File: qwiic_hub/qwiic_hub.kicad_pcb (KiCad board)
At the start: 2 copper layers, 22.8 x 15.6 mm, 10 parts, among them J1 Conn_01x04_Pin, J2 Conn_01x04_Pin, J3 Conn_01x04_Pin, J4 Conn_01x04_Pin, J5 Conn_01x04_Pin, J6 Conn_01x04_Socket, X1 QWIIC Logo

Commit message: Cleaned up the layout.
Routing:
- net /GND: track 51.4 -> 55.5 mm
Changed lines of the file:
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@@
     (fp_line (start 3 -1.675) (end 3 2.575)
       (stroke (width 0.1) (type solid)) (layer "F.Fab"))
-    (pad "1" smd roundrect (at -1.5 -2 90) (size 0.6 1.55) (layers "F.Cu" "F.Paste" "F.Mask") (roundrect_rratio 0.25)
+    (pad "1" thru_hole roundrect (at -1.5 -2 90) (size 0.6 1.55) (drill 0.3) (layers "*.Cu" "F.Paste" "F.Mask") (roundrect_rratio 0.25)
       (net 4 "/GND") (pinfunction "Pin_1") (pintype "passive"))
-    (pad "2" smd roundrect (at -0.5 -2 90) (size 0.6 1.55) (layers "F.Cu" "F.Paste" "F.Mask") (roundrect_rratio 0.25)
+    (pad "2" thru_hole roundrect (at -0.5 -2 90) (size 0.6 1.55) (drill 0.3) (layers "*.Cu" "F.Paste" "F.Mask") (roundrect_rratio 0.25)
       (net 6 "Net-(J1-Pin_2)") (pinfunction "Pin_2") (pintype "passive"))
-    (pad "3" smd roundrect (at 0.5 -2 90) (size 0.6 1.55) (layers "F.Cu" "F.Paste" "F.Mask") (roundrect_rratio 0.25)
+    (pad "3" thru_hole roundrect (at 0.5 -2 90) (size 0.6 1.55) (drill 0.3) (layers "*.Cu" "F.Paste" "F.Mask") (roundrect_rratio 0.25)
       (net 2 "Net-(J1-Pin_3)") (pinfunction "Pin_3") (pintype "passive"))
-    (pad "4" smd roundrect (at 1.5 -2 90) (size 0.6 1.55) (layers "F.Cu" "F.Paste" "F.Mask") (roundrect_rratio 0.25)
+    (pad "4" thru_hole roundrect (at 1.5 -2 90) (size 0.6 1.55) (drill 0.3) (layers "*.Cu" "F.Paste" "F.Mask") (roundrect_rratio 0.25)
       (net 3 "Net-(J1-Pin_4)") (pinfunction "Pin_4") (pintype "passive"))
-    (pad "MP" smd roundrect (at -2.8 1.875 90) (size 1.2 1.8) (layers "F.Cu" "F.Paste" "F.Mask") (roundrect_rratio 0.2083333333))
-    (pad "MP" smd roundrect (at 2.8 1.875 90) (size 1.2 1.8) (layers "F.Cu" "F.Paste" "F.Mask") (roundrect_rratio 0.2083333333))
+    (pad "MP" thru_hole roundrect (at -2.8 1.875 90) (size 1.2 1.8) (drill 0.3) (layers "*.Cu" "F.Paste" "F.Mask") (roundrect_rratio 0.2083333333))
+    (pad "MP" thru_hole roundrect (at 2.8 1.875 90) (size 1.2 1.8) (drill 0.3) (layers "*.Cu" "F.Paste" "F.Mask") (roundrect_rratio 0.2083333333))
     (model "${KICAD6_3DMODEL_DIR}/Connector_JST.3dshapes/JST_SH_SM04B-SRSS-TB_1x04-1MP_P1.00mm_Horizontal.wrl"
       (offset (xyz 0 0 0))
@@
   (segment (start 148.6662 86.3219) (end 148.6662 82.3341) (width 0.3048) (layer "B.Cu") (net 3))
   (segment (start 147.3962 85.3412) (end 147.375 85.32) (width 0.3048) (layer "F.Cu") (net 4))
-  (segment (start 149.287 92.7562) (end 148.0312 92.7562) (width 0.3048) (layer "F.Cu") (net 4))
   (segment (start 139.7254 85.3186) (end 139.7268 85.32) (width 0.3048) (layer "F.Cu") (net 4))
   (segment (start 135.945 85.32) (end 139.724 85.32) (width 0.3048) (layer "F.Cu") (net 4))
   (segment (start 135.945 89.0228) (end 133.985 90.9828) (width 0.3048) (layer "F.Cu") (net 4))
   (segment (start 139.7268 85.32) (end 153.09 85.32) (width 0.3048) (layer "F.Cu") (net 4))
+  (segment (start 151.0492 92.7562) (end 151.0538 92.7608) (width 0.3048) (layer "F.Cu") (net 4))
+  (segment (start 149.287 93.4862) (end 148.971 93.8022) (width 0.3048) (layer "F.Cu") (net 4))
   (segment (start 139.724 85.32) (end 139.7254 85.3186) (width 0.3048) (layer "F.Cu") (net 4))
-  (segment (start 149.287 92.7562) (end 150.7698 92.7562) (width 0.3048) (layer "F.Cu") (net 4))
+  (segment (start 149.287 92.7562) (end 149.287 93.4862) (width 0.3048) (layer "F.Cu") (net 4))
   (segment (start 133.985 90.9828) (end 133.985 93.98) (width 0.3048) (layer "F.Cu") (net 4))
   (segment (start 145.41495 94.6404) (end 144.34825 94.6404) (width 0.3048) (layer "F.Cu") (net 4))
   (segment (start 135.945 85.32) (end 135.945 89.0228) (width 0.3048) (layer "F.Cu") (net 4))
-  (segment (start 150.7698 92.7562) (end 150.7744 92.7608) (width 0.3048) (layer "F.Cu") (net 4))
-  (via (at 150.7744 92.7608) (size 1.016) (drill 0.508) (layers "F.Cu" "B.Cu") (net 4))
-  (via (at 148.082 92.7562) (size 1.016) (drill 0.508) (layers "F.Cu" "B.Cu") (net 4))
+  (segment (start 149.287 92.7562) (end 151.0492 92.7562) (width 0.3048) (layer "F.Cu") (net 4))
+  (segment (start 148.971 93.8022) (end 147.9804 93.8022) (width 0.3048) (layer "F.Cu") (net 4))
+  (via (at 151.0538 92.7608) (size 1.016) (drill 0.508) (layers "F.Cu" "B.Cu") (net 4))
+  (via (at 147.9804 93.8022) (size 1.016) (drill 0.508) (layers "F.Cu" "B.Cu") (net 4))
   (via (at 145.542 94.6404) (size 0.762) (drill 0.381) (layers "F.Cu" "B.Cu") (net 4))
-  (segment (start 147.375 85.32) (end 147.375 90.115) (width 0.3048) (layer "B.Cu") (net 4))
-  (segment (start 153.09 85.32) (end 153.09 90.8262) (width 0.3048) (layer "B.Cu") (net 4))
-  (segment (start 135.9408 85.3242) (end 135.9408 90.2462) (width 0.3048) (layer "B.Cu") (net 4))
+  (segment (start 147.375 85.32) (end 147.375 91.0802) (width 0.3048) (layer "B.Cu") (net 4))
+  (segment (start 153.09 86.3304) (end 151.6634 87.757) (width 0.3048) (layer "B.Cu") (net 4))
+  (segment (start 135.9408 85.3242) (end 135.9408 91.1352) (width 0.3048) (layer "B.Cu") (net 4))
+  (segment (start 153.09 85.32) (end 153.09 86.3304) (width 0.3048) (layer "B.Cu") (net 4))
   (segment (start 141.66 90.9786) (end 141.6558 90.9828) (width 0.3048) (layer "B.Cu") (net 4))
+  (segment (start 151.6634 87.757) (end 151.6634 91.3384) (width 0.3048) (layer "B.Cu") (net 4))
   (segment (start 141.66 85.32) (end 141.66 90.9786) (width 0.3048) (layer "B.Cu") (net 4))
-  (segment (start 147.375 90.115) (end 147.3708 90.1192) (width 0.3048) (layer "B.Cu") (net 4))
   (segment (start 135.945 85.32) (end 135.9408 85.3242) (width 0.3048) (layer "B.Cu") (net 4))
-  (segment (start 153.09 90.8262) (end 153.0858 90.8304) (width 0.3048) (layer "B.Cu") (net 4))
+  (segment (start 147.375 91.0802) (end 147.3454 91.1098) (width 0.3048) (layer "B.Cu") (net 4))
   (segment (start 136.525 90.3732) (end 136.525 93.98) (width 0.3048) (layer "F.Cu") (net 5))
   (segment (start 144.907 90.4494) (end 144.907 88.138) (width 0.3048) (layer "F.Cu") (net 5))
@@
   (via (at 137.3886 86.4362) (size 1.016) (drill 0.508) (layers "F.Cu" "B.Cu") (net 5))
   (via (at 137.3632 84.328) (size 1.016) (drill 0.508) (layers "F.Cu" "B.Cu") (net 5))
-  (via (at 144.8054 88.0364) (size 1.016) (drill 0.508) (layers "F.Cu" "B.Cu") (net 5))
+  (via (at 144.907 88.0364) (size 1.016) (drill 0.508) (layers "F.Cu" "B.Cu") (net 5))
+  (segment (start 144.8054 88.0364) (end 144.1196 88.0364) (width 0.3048) (layer "B.Cu") (net 5))
+  (segment (start 143.5976 87.5144) (end 143.5976 84.9516) (width 0.3048) (layer "B.Cu") (net 5))
+  (segment (start 137.3632 84.328) (end 137.3632 86.4108) (width 0.3048) (layer "B.Cu") (net 5))
+  (segment (start 144.1196 88.0364) (end 143.5976 87.5144) (width 0.3048) (layer "B.Cu") (net 5))
+  (segment (start 137.3632 86.4108) (end 137.3886 86.4362) (width 0.3048) (layer "B.Cu") (net 5))
   (segment (start 143.5976 84.9516) (end 144.2212 84.328) (width 0.3048) (layer "B.Cu") (net 5))
-  (segment (start 137.3632 84.328) (end 137.3632 86.4108) (width 0.3048) (layer "B.Cu") (net 5))
-  (segment (start 143.5976 87.3112) (end 143.5976 84.9516) (width 0.3048) (layer "B.Cu") (net 5))
-  (segment (start 137.3632 86.4108) (end 137.3886 86.4362) (width 0.3048) (layer "B.Cu") (net 5))
-  (segment (start 144.8054 88.0364) (end 144.3228 88.0364) (width 0.3048) (layer "B.Cu") (net 5))
-  (segment (start 144.3228 88.0364) (end 143.5976 87.3112) (width 0.3048) (layer "B.Cu") (net 5))
   (segment (start 146.7648 91.7562) (end 146.6596 91.8614) (width 0.3048) (layer "F.Cu") (net 6))
   (segment (start 149.287 91.7562) (end 146.7648 91.7562) (width 0.3048) (layer "F.Cu") (net 6))
@@
     (polygon
       (pts
-        (xy 131.0132 89.2302)
-        (xy 155.0924 89.2048)
+        (xy 131.0386 89.6874)
+        (xy 155.1432 89.662)
         (xy 155.1178 96.3422)
         (xy 131.191 96.3422)

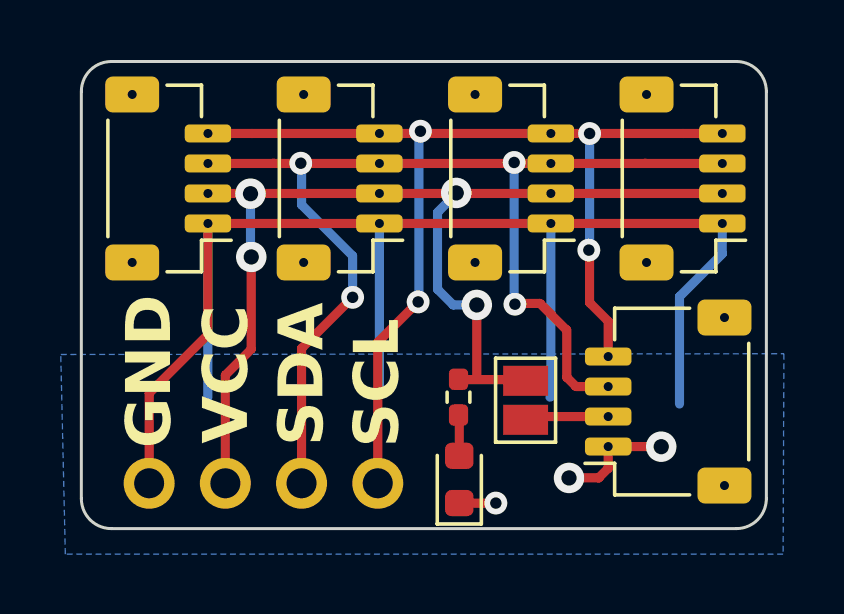
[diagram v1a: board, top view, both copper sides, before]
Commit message: Tweaked the qwiic hub layout.
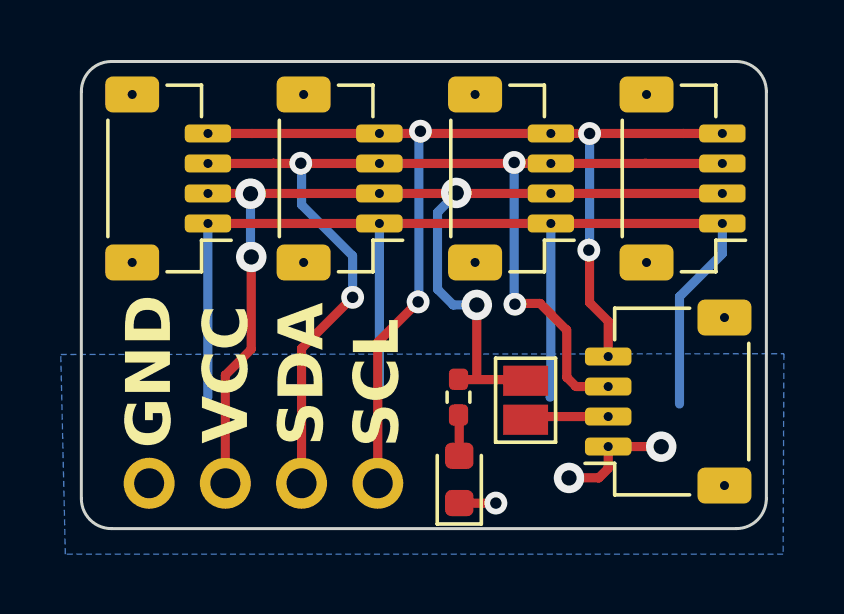
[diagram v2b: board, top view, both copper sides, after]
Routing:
- net /GND: track 55.5 -> 46.1 mm
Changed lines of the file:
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@@
   (segment (start 139.7254 85.3186) (end 139.7268 85.32) (width 0.3048) (layer "F.Cu") (net 4))
   (segment (start 135.945 85.32) (end 139.724 85.32) (width 0.3048) (layer "F.Cu") (net 4))
-  (segment (start 135.945 89.0228) (end 133.985 90.9828) (width 0.3048) (layer "F.Cu") (net 4))
   (segment (start 139.7268 85.32) (end 153.09 85.32) (width 0.3048) (layer "F.Cu") (net 4))
   (segment (start 151.0492 92.7562) (end 151.0538 92.7608) (width 0.3048) (layer "F.Cu") (net 4))
@@
   (segment (start 139.724 85.32) (end 139.7254 85.3186) (width 0.3048) (layer "F.Cu") (net 4))
   (segment (start 149.287 92.7562) (end 149.287 93.4862) (width 0.3048) (layer "F.Cu") (net 4))
-  (segment (start 133.985 90.9828) (end 133.985 93.98) (width 0.3048) (layer "F.Cu") (net 4))
   (segment (start 145.41495 94.6404) (end 144.34825 94.6404) (width 0.3048) (layer "F.Cu") (net 4))
-  (segment (start 135.945 85.32) (end 135.945 89.0228) (width 0.3048) (layer "F.Cu") (net 4))
   (segment (start 149.287 92.7562) (end 151.0492 92.7562) (width 0.3048) (layer "F.Cu") (net 4))
   (segment (start 148.971 93.8022) (end 147.9804 93.8022) (width 0.3048) (layer "F.Cu") (net 4))
